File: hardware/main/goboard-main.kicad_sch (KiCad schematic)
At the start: 8 parts, among them J1 USB_C_Receptacle_USB2.0, J2 Conn_01x05_Female

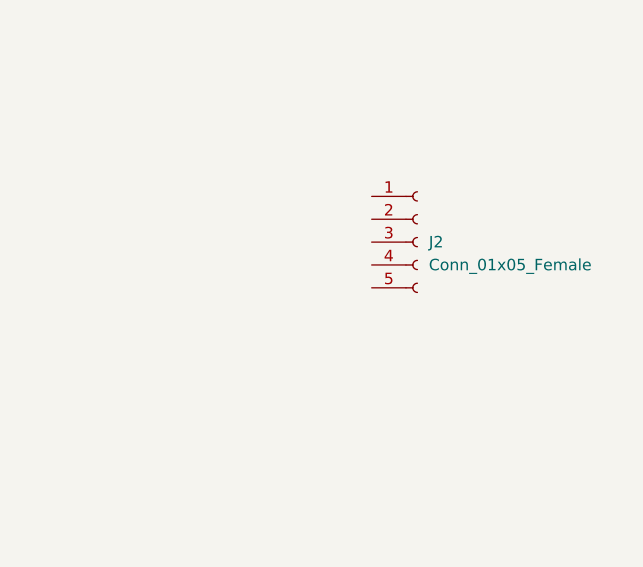
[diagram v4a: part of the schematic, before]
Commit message: Add connector to the numpad to the schematic
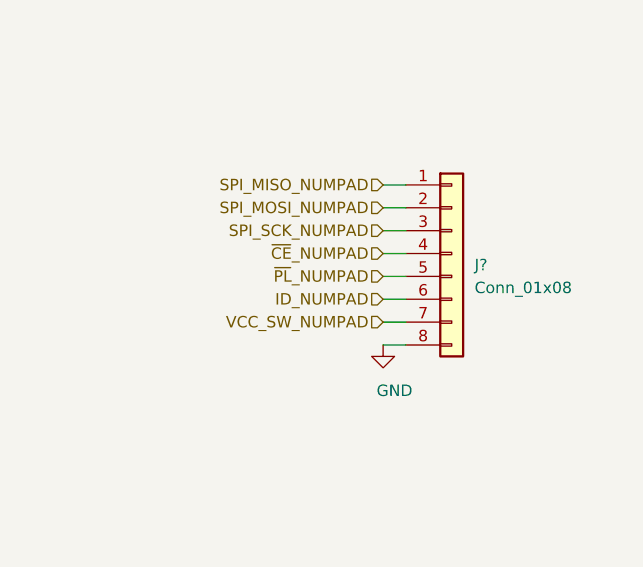
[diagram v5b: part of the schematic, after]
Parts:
- removed J2: Conn_01x05_Female, symbol Connector:Conn_01x05_Female
- added J?: Conn_01x08, symbol Connector_Generic:Conn_01x08
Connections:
- net GND: now also J?.8 (Pin_8)
- new net ID_NUMPAD: J?.6 (Pin_6)
- new net SPI_MISO_NUMPAD: J?.1 (Pin_1)
- new net SPI_MOSI_NUMPAD: J?.2 (Pin_2)
- new net SPI_SCK_NUMPAD: J?.3 (Pin_3)
- new net VCC_SW_NUMPAD: J?.7 (Pin_7)
- new net ~CE~_NUMPAD: J?.4 (Pin_4)
- new net ~PL~_NUMPAD: J?.5 (Pin_5)
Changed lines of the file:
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@@
   (junction (at 80.01 91.44) (diameter 1.016) (color 0 0 0 0))
   (junction (at 86.36 60.96) (diameter 1.016) (color 0 0 0 0))
+  (no_connect (at 41.91 66.04))
   (no_connect (at 41.91 63.5))
-  (no_connect (at 41.91 66.04))
   (wire (pts (xy 19.05 73.66) (xy 19.05 76.2))
     (stroke (width 0) (type solid) (color 0 0 0 0))
@@
   )
   (wire (pts (xy 118.11 45.72) (xy 120.65 45.72))
+    (stroke (width 0) (type solid) (color 0 0 0 0))
+  )
+  (wire (pts (xy 257.81 95.25) (xy 260.35 95.25))
+    (stroke (width 0) (type solid) (color 0 0 0 0))
+  )
+  (wire (pts (xy 257.81 97.79) (xy 260.35 97.79))
+    (stroke (width 0) (type solid) (color 0 0 0 0))
+  )
+  (wire (pts (xy 257.81 100.33) (xy 260.35 100.33))
+    (stroke (width 0) (type solid) (color 0 0 0 0))
+  )
+  (wire (pts (xy 257.81 102.87) (xy 260.35 102.87))
+    (stroke (width 0) (type solid) (color 0 0 0 0))
+  )
+  (wire (pts (xy 257.81 105.41) (xy 260.35 105.41))
+    (stroke (width 0) (type solid) (color 0 0 0 0))
+  )
+  (wire (pts (xy 257.81 107.95) (xy 260.35 107.95))
+    (stroke (width 0) (type solid) (color 0 0 0 0))
+  )
+  (wire (pts (xy 257.81 110.49) (xy 260.35 110.49))
+    (stroke (width 0) (type solid) (color 0 0 0 0))
+  )
+  (wire (pts (xy 257.81 113.03) (xy 260.35 113.03))
     (stroke (width 0) (type solid) (color 0 0 0 0))
   )
@@
     (effects (font (size 1.27 1.27)) (justify right))
   )
+  (hierarchical_label "SPI_MISO_NUMPAD" (shape input) (at 257.81 95.25 180)
+    (effects (font (size 1.27 1.27)) (justify right))
+  )
+  (hierarchical_label "SPI_MOSI_NUMPAD" (shape input) (at 257.81 97.79 180)
+    (effects (font (size 1.27 1.27)) (justify right))
+  )
+  (hierarchical_label "SPI_SCK_NUMPAD" (shape input) (at 257.81 100.33 180)
+    (effects (font (size 1.27 1.27)) (justify right))
+  )
+  (hierarchical_label "~CE~_NUMPAD" (shape input) (at 257.81 102.87 180)
+    (effects (font (size 1.27 1.27)) (justify right))
+  )
+  (hierarchical_label "~PL~_NUMPAD" (shape input) (at 257.81 105.41 180)
+    (effects (font (size 1.27 1.27)) (justify right))
+  )
+  (hierarchical_label "ID_NUMPAD" (shape input) (at 257.81 107.95 180)
+    (effects (font (size 1.27 1.27)) (justify right))
+  )
+  (hierarchical_label "VCC_SW_NUMPAD" (shape input) (at 257.81 110.49 180)
+    (effects (font (size 1.27 1.27)) (justify right))
+  )
   (symbol (lib_id "power:VCC") (at 44.45 35.56 0) (unit 1)
     (in_bom yes) (on_board yes)
@@
     )
     (property "Datasheet" "" (id 3) (at 86.36 63.5 0)
+      (effects (font (size 1.27 1.27)) hide)
+    )
+  )
+  (symbol (lib_id "power:GND") (at 257.81 113.03 0) (unit 1)
+    (in_bom yes) (on_board yes)
+    (property "Reference" "#PWR?" (id 0) (at 257.81 119.38 0)
+      (effects (font (size 1.27 1.27)) hide)
+    )
+    (property "Value" "GND" (id 1) (at 259.08 118.11 0))
+    (property "Footprint" "" (id 2) (at 257.81 113.03 0)
+      (effects (font (size 1.27 1.27)) hide)
+    )
+    (property "Datasheet" "" (id 3) (at 257.81 113.03 0)
       (effects (font (size 1.27 1.27)) hide)
     )
@@
     )
   )
-  (symbol (lib_id "Connector:Conn_01x05_Female") (at 261.62 101.6 0) (unit 1)
-    (in_bom yes) (on_board yes)
-    (property "Reference" "J2" (id 0) (at 262.89 101.6 0)
-      (effects (font (size 1.27 1.27)) (justify left))
-    )
-    (property "Value" "Conn_01x05_Female" (id 1) (at 262.89 104.14 0)
-      (effects (font (size 1.27 1.27)) (justify left))
-    )
-    (property "Footprint" "" (id 2) (at 261.62 101.6 0)
-      (effects (font (size 1.27 1.27)) hide)
-    )
-    (property "Datasheet" "~" (id 3) (at 261.62 101.6 0)
+  (symbol (lib_id "Connector_Generic:Conn_01x08") (at 265.43 102.87 0) (unit 1)
+    (in_bom yes) (on_board yes)
+    (property "Reference" "J?" (id 0) (at 267.97 104.14 0)
+      (effects (font (size 1.27 1.27)) (justify left))
+    )
+    (property "Value" "Conn_01x08" (id 1) (at 267.97 106.68 0)
+      (effects (font (size 1.27 1.27)) (justify left))
+    )
+    (property "Footprint" "" (id 2) (at 265.43 102.87 0)
+      (effects (font (size 1.27 1.27)) hide)
+    )
+    (property "Datasheet" "~" (id 3) (at 265.43 102.87 0)
       (effects (font (size 1.27 1.27)) hide)
     )
@@
       (effects (font (size 1.27 1.27)) hide)
     )
-    (property "Datasheet" "https://www.mouser.de/datasheet/2/206/JAE_Electronics_01282020_DX07-1729578.pdf" (id 3) (at 30.48 50.8 0)
+    (property "Datasheet" "https://www.usb.org/sites/default/files/documents/usb_type-c.zip" (id 3) (at 30.48 50.8 0)
       (effects (font (size 1.27 1.27)) hide)
     )
@@
       (reference "#PWR0108") (unit 1) (value "VCC") (footprint "")
     )
+    (path "/8b13a53d-02e2-4844-8c3e-665bfacdc66a"
+      (reference "#PWR?") (unit 1) (value "GND") (footprint "")
+    )
     (path "/d7e33325-4578-4e92-bf2f-a87bebb610ba"
       (reference "C1") (unit 1) (value "100nF") (footprint "")
@@
       (reference "J1") (unit 1) (value "USB_C_Receptacle_USB2.0") (footprint "footprints:USB_C_Receptale_JAE_DX07S016JA1R1500")
     )
-    (path "/791bf4bc-b52e-43a7-af69-54454aa52998"
-      (reference "J2") (unit 1) (value "Conn_01x05_Female") (footprint "")
+    (path "/a1c93486-cda7-4488-8ee1-9e8f3097e66e"
+      (reference "J?") (unit 1) (value "Conn_01x08") (footprint "")
     )
     (path "/70bfc3f4-60ca-4487-a365-ec787e69545b"

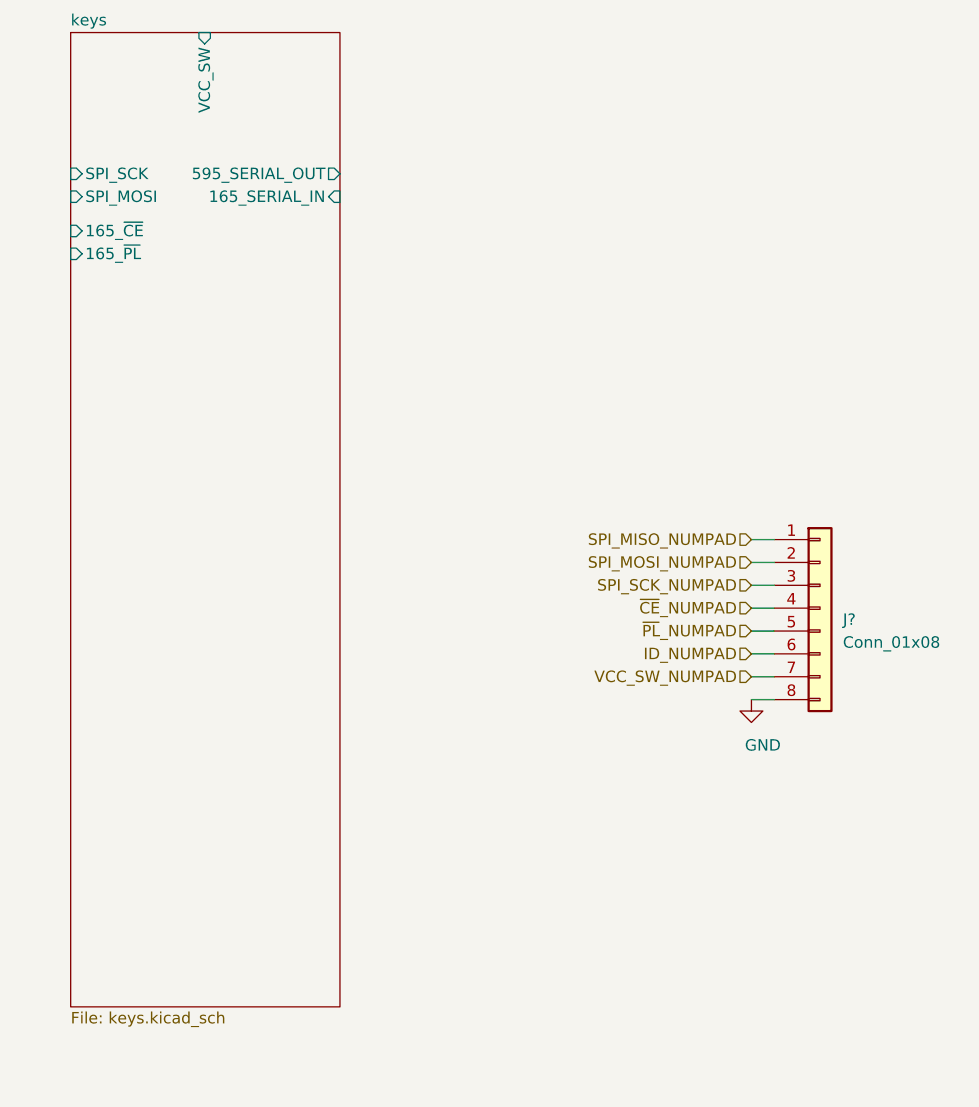
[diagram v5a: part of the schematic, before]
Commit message: Modify the connection to the numpad
As the numpad now uses a stm-microcontroller instead of the
shift-registers the connection is changed to UART.
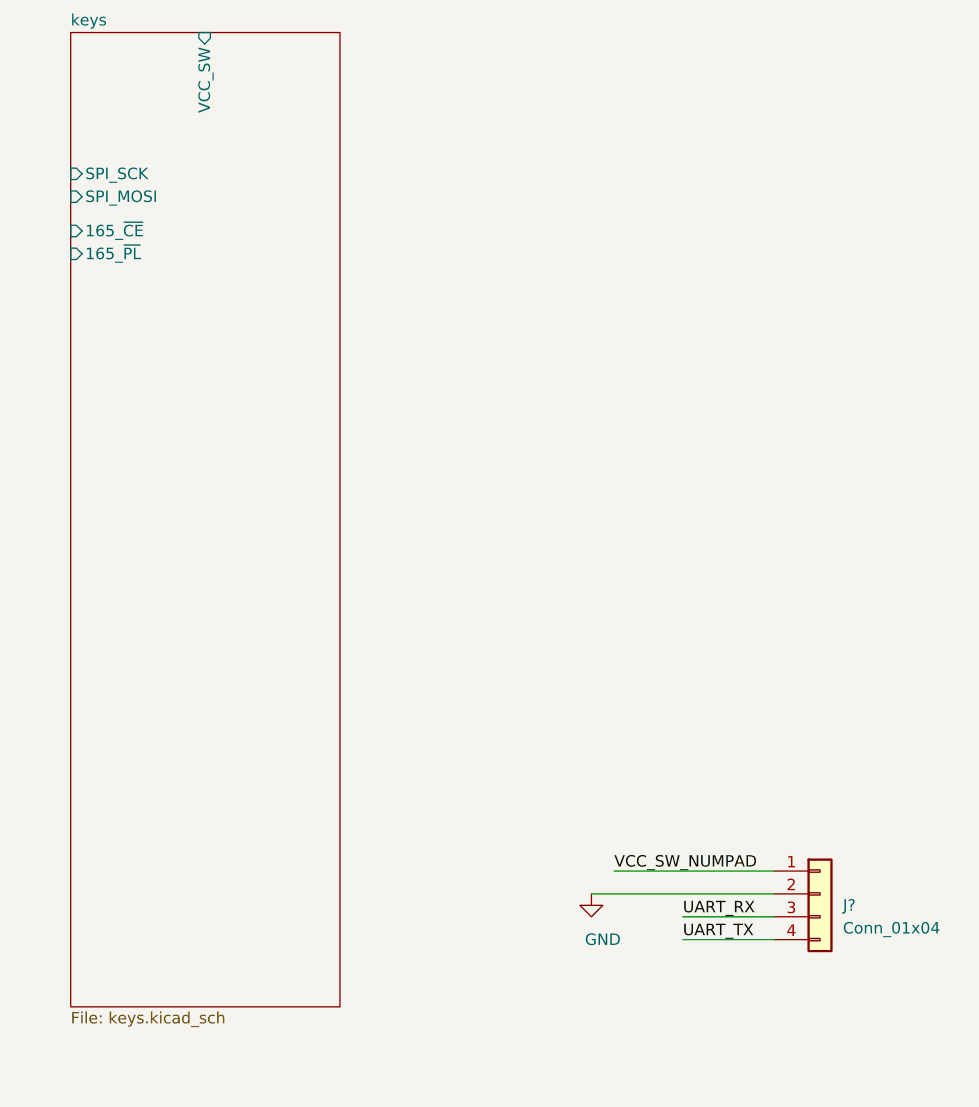
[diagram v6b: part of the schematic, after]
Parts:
- removed J?: Conn_01x08, symbol Connector_Generic:Conn_01x08
- added J?: Conn_01x04, symbol Connector_Generic:Conn_01x04
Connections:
- net GND: now also J?.2 (Pin_2)
- net VCC_SW_NUMPAD: now also J?.1 (Pin_1)
- new net UART_RX: J?.3 (Pin_3)
- new net UART_TX: J?.4 (Pin_4)
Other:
- sheet keys ports: added none; removed 165_SERIAL_IN, 595_SERIAL_OUT
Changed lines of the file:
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@@
     (stroke (width 0) (type solid) (color 0 0 0 0))
   )
-  (wire (pts (xy 257.81 95.25) (xy 260.35 95.25))
-    (stroke (width 0) (type solid) (color 0 0 0 0))
-  )
-  (wire (pts (xy 257.81 97.79) (xy 260.35 97.79))
-    (stroke (width 0) (type solid) (color 0 0 0 0))
-  )
-  (wire (pts (xy 257.81 100.33) (xy 260.35 100.33))
-    (stroke (width 0) (type solid) (color 0 0 0 0))
-  )
-  (wire (pts (xy 257.81 102.87) (xy 260.35 102.87))
-    (stroke (width 0) (type solid) (color 0 0 0 0))
-  )
-  (wire (pts (xy 257.81 105.41) (xy 260.35 105.41))
-    (stroke (width 0) (type solid) (color 0 0 0 0))
-  )
-  (wire (pts (xy 257.81 107.95) (xy 260.35 107.95))
-    (stroke (width 0) (type solid) (color 0 0 0 0))
-  )
-  (wire (pts (xy 257.81 110.49) (xy 260.35 110.49))
-    (stroke (width 0) (type solid) (color 0 0 0 0))
-  )
-  (wire (pts (xy 257.81 113.03) (xy 260.35 113.03))
+  (wire (pts (xy 240.03 134.62) (xy 260.35 134.62))
+    (stroke (width 0) (type solid) (color 0 0 0 0))
+  )
+  (wire (pts (xy 242.57 132.08) (xy 260.35 132.08))
+    (stroke (width 0) (type solid) (color 0 0 0 0))
+  )
+  (wire (pts (xy 250.19 137.16) (xy 260.35 137.16))
+    (stroke (width 0) (type solid) (color 0 0 0 0))
+  )
+  (wire (pts (xy 250.19 139.7) (xy 260.35 139.7))
     (stroke (width 0) (type solid) (color 0 0 0 0))
   )
@@
     (effects (font (size 1.27 1.27)) (justify left bottom))
   )
+  (label "VCC_SW_NUMPAD" (at 242.57 132.08 0)
+    (effects (font (size 1.27 1.27)) (justify left bottom))
+  )
+  (label "UART_RX" (at 250.19 137.16 0)
+    (effects (font (size 1.27 1.27)) (justify left bottom))
+  )
+  (label "UART_TX" (at 250.19 139.7 0)
+    (effects (font (size 1.27 1.27)) (justify left bottom))
+  )
   (hierarchical_label "USB_D-" (shape input) (at 54.61 49.53 0)
     (effects (font (size 1.27 1.27)) (justify left))
@@
     (effects (font (size 1.27 1.27)) (justify right))
   )
-  (hierarchical_label "SPI_MISO_NUMPAD" (shape input) (at 257.81 95.25 180)
-    (effects (font (size 1.27 1.27)) (justify right))
-  )
-  (hierarchical_label "SPI_MOSI_NUMPAD" (shape input) (at 257.81 97.79 180)
-    (effects (font (size 1.27 1.27)) (justify right))
-  )
-  (hierarchical_label "SPI_SCK_NUMPAD" (shape input) (at 257.81 100.33 180)
-    (effects (font (size 1.27 1.27)) (justify right))
-  )
-  (hierarchical_label "~CE~_NUMPAD" (shape input) (at 257.81 102.87 180)
-    (effects (font (size 1.27 1.27)) (justify right))
-  )
-  (hierarchical_label "~PL~_NUMPAD" (shape input) (at 257.81 105.41 180)
-    (effects (font (size 1.27 1.27)) (justify right))
-  )
-  (hierarchical_label "ID_NUMPAD" (shape input) (at 257.81 107.95 180)
-    (effects (font (size 1.27 1.27)) (justify right))
-  )
-  (hierarchical_label "VCC_SW_NUMPAD" (shape input) (at 257.81 110.49 180)
-    (effects (font (size 1.27 1.27)) (justify right))
-  )
   (symbol (lib_id "power:VCC") (at 44.45 35.56 0) (unit 1)
     (in_bom yes) (on_board yes)
@@
     )
   )
-  (symbol (lib_id "power:GND") (at 257.81 113.03 0) (unit 1)
-    (in_bom yes) (on_board yes)
-    (property "Reference" "#PWR?" (id 0) (at 257.81 119.38 0)
-      (effects (font (size 1.27 1.27)) hide)
-    )
-    (property "Value" "GND" (id 1) (at 259.08 118.11 0))
-    (property "Footprint" "" (id 2) (at 257.81 113.03 0)
-      (effects (font (size 1.27 1.27)) hide)
-    )
-    (property "Datasheet" "" (id 3) (at 257.81 113.03 0)
+  (symbol (lib_id "power:GND") (at 240.03 134.62 0) (unit 1)
+    (in_bom yes) (on_board yes)
+    (property "Reference" "#PWR?" (id 0) (at 240.03 140.97 0)
+      (effects (font (size 1.27 1.27)) hide)
+    )
+    (property "Value" "GND" (id 1) (at 241.3 139.7 0))
+    (property "Footprint" "" (id 2) (at 240.03 134.62 0)
+      (effects (font (size 1.27 1.27)) hide)
+    )
+    (property "Datasheet" "" (id 3) (at 240.03 134.62 0)
       (effects (font (size 1.27 1.27)) hide)
     )
@@
     )
   )
-  (symbol (lib_id "Connector_Generic:Conn_01x08") (at 265.43 102.87 0) (unit 1)
-    (in_bom yes) (on_board yes)
-    (property "Reference" "J?" (id 0) (at 267.97 104.14 0)
-      (effects (font (size 1.27 1.27)) (justify left))
-    )
-    (property "Value" "Conn_01x08" (id 1) (at 267.97 106.68 0)
-      (effects (font (size 1.27 1.27)) (justify left))
-    )
-    (property "Footprint" "" (id 2) (at 265.43 102.87 0)
-      (effects (font (size 1.27 1.27)) hide)
-    )
-    (property "Datasheet" "~" (id 3) (at 265.43 102.87 0)
+  (symbol (lib_id "Connector_Generic:Conn_01x04") (at 265.43 134.62 0) (unit 1)
+    (in_bom yes) (on_board yes)
+    (property "Reference" "J?" (id 0) (at 267.97 135.89 0)
+      (effects (font (size 1.27 1.27)) (justify left))
+    )
+    (property "Value" "Conn_01x04" (id 1) (at 267.97 138.43 0)
+      (effects (font (size 1.27 1.27)) (justify left))
+    )
+    (property "Footprint" "" (id 2) (at 265.43 134.62 0)
+      (effects (font (size 1.27 1.27)) hide)
+    )
+    (property "Datasheet" "~" (id 3) (at 265.43 134.62 0)
       (effects (font (size 1.27 1.27)) hide)
     )
@@
       (effects (font (size 1.27 1.27)) (justify left))
     )
-    (pin "595_SERIAL_OUT" output (at 212.09 54.61 0)
-      (effects (font (size 1.27 1.27)) (justify right))
-    )
-    (pin "165_SERIAL_IN" input (at 212.09 57.15 0)
-      (effects (font (size 1.27 1.27)) (justify right))
-    )
   )
   (sheet_instances
@@
       (reference "#PWR0108") (unit 1) (value "VCC") (footprint "")
     )
-    (path "/8b13a53d-02e2-4844-8c3e-665bfacdc66a"
+    (path "/b53f266a-100b-4c6f-9ed7-0ad25cdc4b2e"
       (reference "#PWR?") (unit 1) (value "GND") (footprint "")
     )
@@
       (reference "J1") (unit 1) (value "USB_C_Receptacle_USB2.0") (footprint "footprints:USB_C_Receptale_JAE_DX07S016JA1R1500")
     )
-    (path "/a1c93486-cda7-4488-8ee1-9e8f3097e66e"
-      (reference "J?") (unit 1) (value "Conn_01x08") (footprint "")
+    (path "/45dbaac3-8890-4544-bcad-241b4dfd7df9"
+      (reference "J?") (unit 1) (value "Conn_01x04") (footprint "")
     )
     (path "/70bfc3f4-60ca-4487-a365-ec787e69545b"

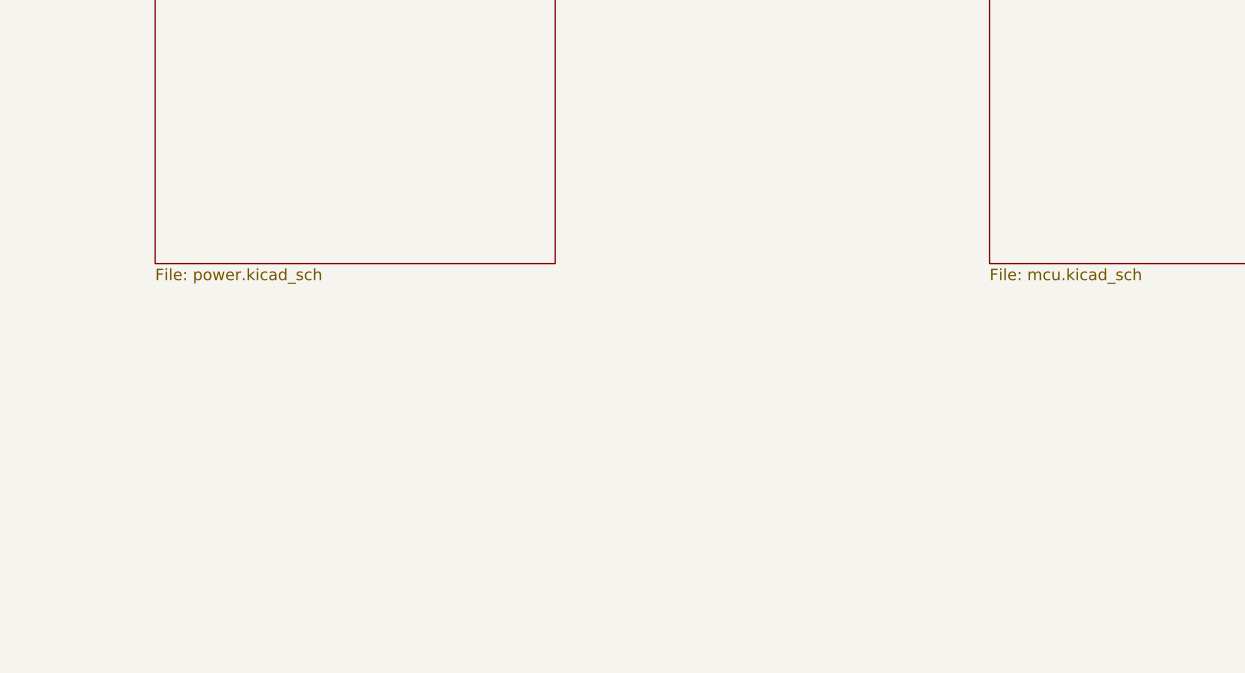
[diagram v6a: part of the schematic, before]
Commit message: Add programming/debug connection
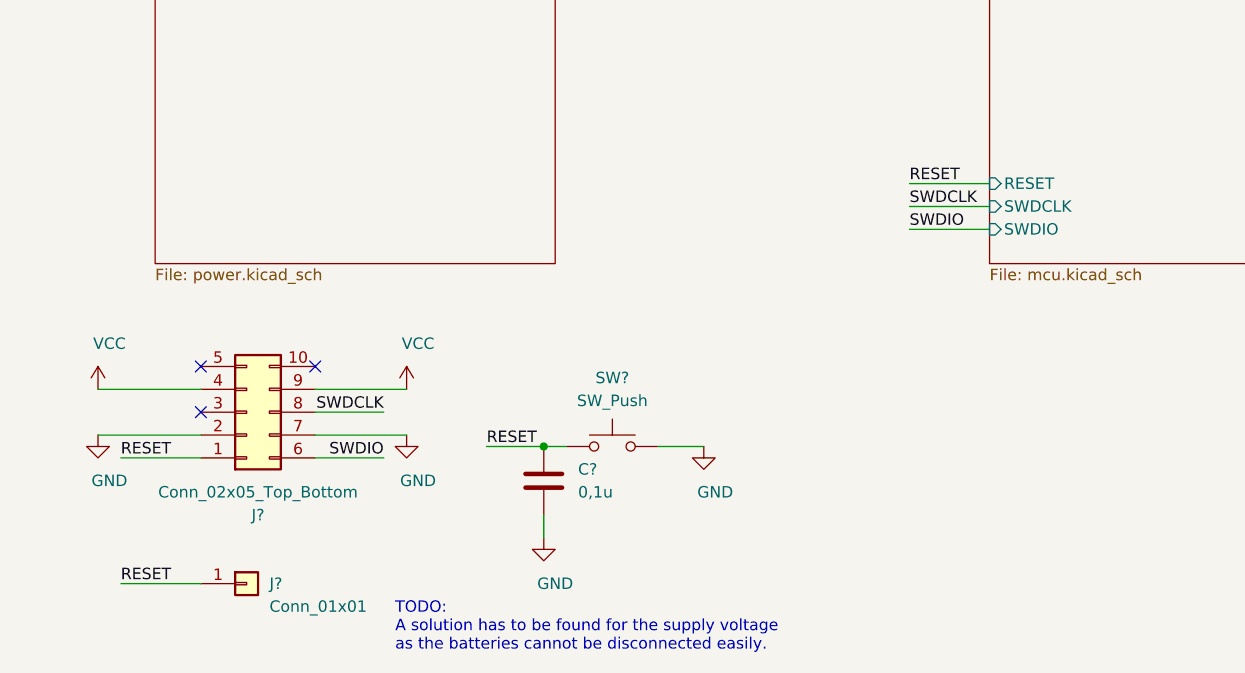
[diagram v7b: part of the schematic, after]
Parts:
- added C?: 0,1u, symbol Device:C
- added J?: Conn_02x05_Top_Bottom, symbol Connector_Generic:Conn_02x05_Top_Bottom
- added J?: Conn_01x01, symbol Connector_Generic:Conn_01x01
- added SW?: SW_Push, symbol Switch:SW_Push
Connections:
- net GND: now also C?.2, J?.2 (Pin_2), J?.7 (Pin_7), SW?.2
- net VCC: now also J?.4 (Pin_4), J?.9 (Pin_9)
- new net RESET: C?.1, J?.1 (Pin_1), J?.1 (Pin_1), SW?.1
- new net SWDCLK: J?.8 (Pin_8)
- new net SWDIO: J?.6 (Pin_6)
- no-connect marks 2 -> 5
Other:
- sheet MCU ports: added RESET, SWDCLK, SWDIO; removed none
- note added: "TODO: A solution has to be found for the supply voltage as the batteries cannot be disconnected easily."
